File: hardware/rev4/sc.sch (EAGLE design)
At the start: 88 parts, among them IC1 PB137ACV, IC2 LM2675M-ADJ, Q1 si2305cd, Q2 IRFR5305, Q3 IRFR5305, T1 BC846, T2 BC846, T3 BC846, U1 SPX5205 3v3, X1 prog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

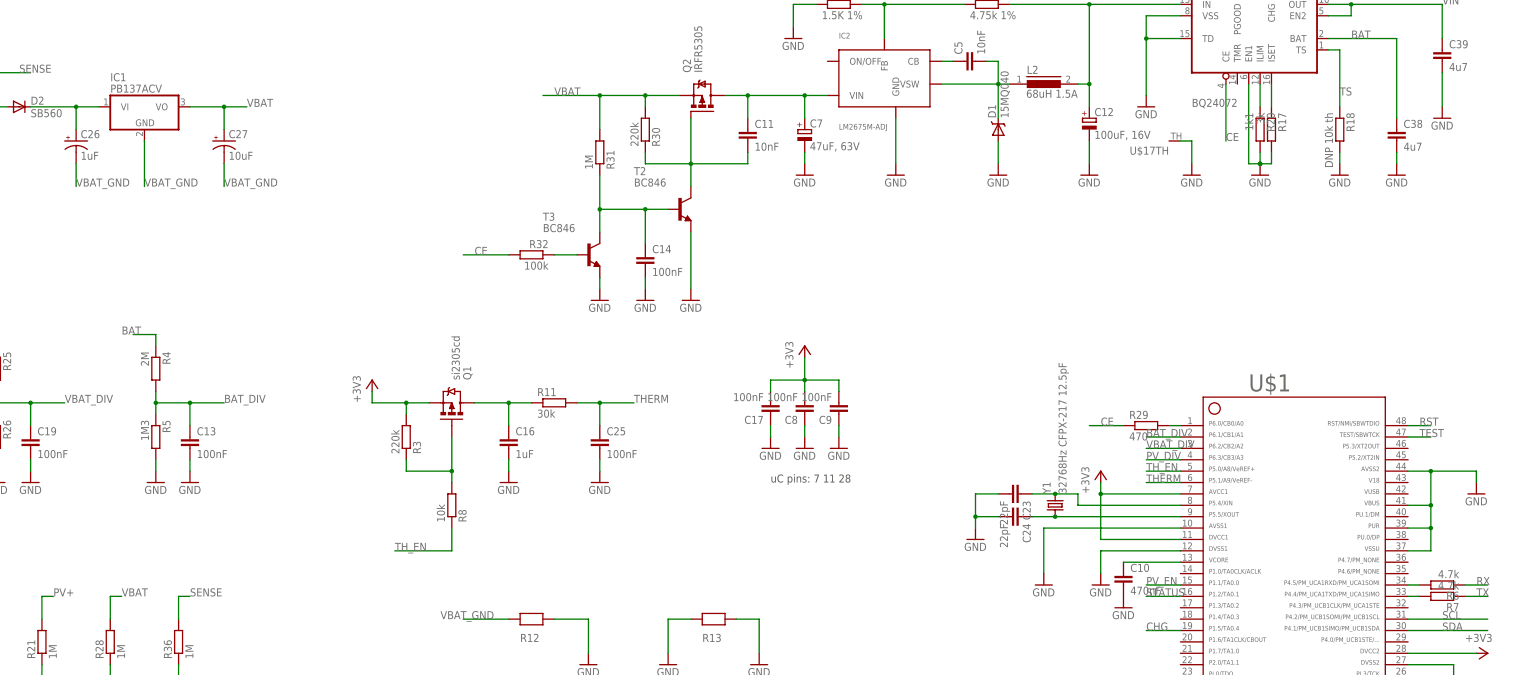
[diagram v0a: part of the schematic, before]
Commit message: control pins working
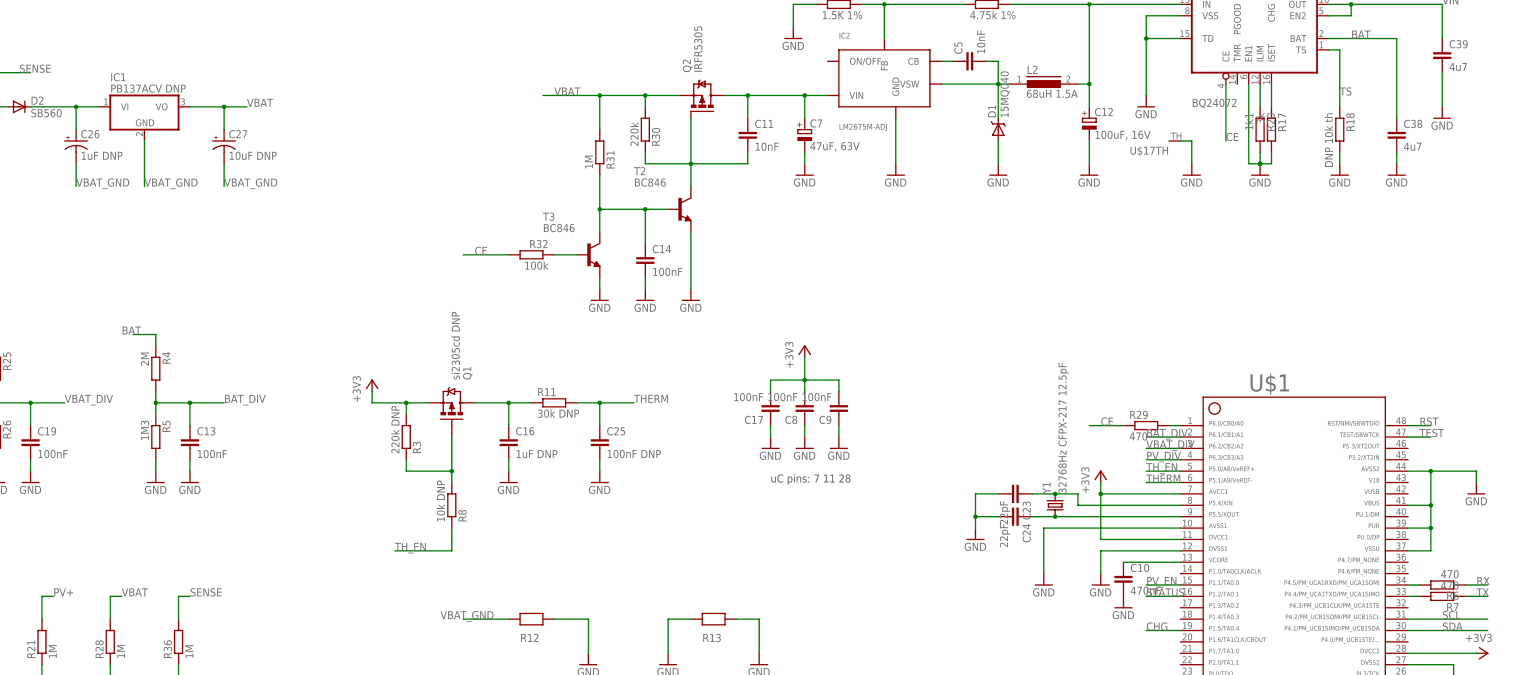
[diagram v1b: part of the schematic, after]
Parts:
- C16, C26: value 1uF -> 1uF DNP
- C25: value 100nF -> 100nF DNP
- C27: value 10uF -> 10uF DNP
- IC1: value PB137ACV -> PB137ACV DNP
- Q1: value si2305cd -> si2305cd DNP
- R11: value 30k -> 30k DNP
- R3: value 220k -> 220k DNP
- R6, R7: value 4.7k -> 470
- R8: value 10k -> 10k DNP
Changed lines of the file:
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@@
 <part name="GND22" library="SparkFun" deviceset="GND" device=""/>
 <part name="C10" library="rcl" deviceset="C-EU" device="C0805" value="470nF"/>
-<part name="R6" library="rcl" deviceset="R-EU_" device="R0805W" value="4.7k"/>
-<part name="R7" library="rcl" deviceset="R-EU_" device="R0805W" value="4.7k"/>
+<part name="R6" library="rcl" deviceset="R-EU_" device="R0805W" value="470"/>
+<part name="R7" library="rcl" deviceset="R-EU_" device="R0805W" value="470"/>
 <part name="Y1" library="Simplex-FreqCtrl" deviceset="CRYSTAL" device="3.2X1.5" value="32768Hz CFPX-217 12.5pF"/>
 <part name="C23" library="rcl" deviceset="C-EU" device="C0805" value="22pF"/>
@@
 <part name="R26" library="rcl" deviceset="R-EU_" device="R0805W" value="330k"/>
 <part name="GND34" library="SparkFun" deviceset="GND" device=""/>
-<part name="R3" library="rcl" deviceset="R-EU_" device="R0805W" value="220k"/>
-<part name="Q1" library="Simplex-DiscreteSemi" deviceset="MOSFET-PCHANNEL" device="SMD_POWER" value="si2305cd"/>
-<part name="R8" library="rcl" deviceset="R-EU_" device="R0805W" value="10k"/>
+<part name="R3" library="rcl" deviceset="R-EU_" device="R0805W" value="220k DNP"/>
+<part name="Q1" library="Simplex-DiscreteSemi" deviceset="MOSFET-PCHANNEL" device="SMD_POWER" value="si2305cd DNP"/>
+<part name="R8" library="rcl" deviceset="R-EU_" device="R0805W" value="10k DNP"/>
 <part name="C17" library="rcl" deviceset="C-EU" device="C0805" value="100nF"/>
 <part name="GND32" library="SparkFun" deviceset="GND" device=""/>
@@
 <part name="GND40" library="SparkFun" deviceset="GND" device=""/>
 <part name="GND41" library="SparkFun" deviceset="GND" device=""/>
-<part name="IC1" library="linear" deviceset="78*" device="TV" technology="12" value="PB137ACV"/>
+<part name="IC1" library="linear" deviceset="78*" device="TV" technology="12" value="PB137ACV DNP"/>
 <part name="Q3" library="transistor-power" deviceset="IRF?5305" device="R"/>
 <part name="R2" library="rcl" deviceset="R-EU_" device="R0805W" value="10k"/>
-<part name="R11" library="rcl" deviceset="R-EU_" device="R0805W" value="30k"/>
-<part name="C25" library="rcl" deviceset="C-EU" device="C0805" value="100nF"/>
+<part name="R11" library="rcl" deviceset="R-EU_" device="R0805W" value="30k DNP"/>
+<part name="C25" library="rcl" deviceset="C-EU" device="C0805" value="100nF DNP"/>
 <part name="GND8" library="SparkFun" deviceset="GND" device=""/>
 <part name="JP2" library="SparkFun-Connectors" deviceset="M02" device="PTH" value="thermistor"/>
-<part name="C27" library="SparkFun-Capacitors" deviceset="CAP_POL" device="D" value="10uF"/>
-<part name="C26" library="SparkFun-Capacitors" deviceset="CAP_POL" device="D" value="1uF"/>
+<part name="C27" library="SparkFun-Capacitors" deviceset="CAP_POL" device="D" value="10uF DNP"/>
+<part name="C26" library="SparkFun-Capacitors" deviceset="CAP_POL" device="D" value="1uF DNP"/>
 <part name="R21" library="rcl" deviceset="R-EU_" device="R0805W" value="1M"/>
 <part name="LED6" library="led" deviceset="LED" device="CHIP-LED0805" value="green"/>
@@
 <part name="Q2" library="transistor-power" deviceset="IRF?5305" device="R"/>
 <part name="GND15" library="SparkFun" deviceset="GND" device=""/>
-<part name="C16" library="rcl" deviceset="C-EU" device="C0805" value="1uF"/>
+<part name="C16" library="rcl" deviceset="C-EU" device="C0805" value="1uF DNP"/>
 <part name="R23" library="rcl" deviceset="R-EU_" device="R0805W" value="4.7k"/>
 <part name="R27" library="rcl" deviceset="R-EU_" device="R0805W" value="4.7k"/>

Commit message: adc, rtc work
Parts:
- R22: value 2M -> 1M2
- R24: value 220k -> 100k
- R32: value 100k -> DNP 100k
- R4: value 2M -> 680K
- R5: value 1M3 -> 330k
- R9: value 4.75k 1% -> 4K3
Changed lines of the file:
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@@
 <part name="R16" library="rcl" deviceset="R-EU_" device="R0805W" value="100k"/>
 <part name="R19" library="rcl" deviceset="R-EU_" device="R0805W" value="220k"/>
-<part name="R22" library="rcl" deviceset="R-EU_" device="R0805W" value="2M"/>
-<part name="R24" library="rcl" deviceset="R-EU_" device="R0805W" value="220k"/>
+<part name="R22" library="rcl" deviceset="R-EU_" device="R0805W" value="1M2"/>
+<part name="R24" library="rcl" deviceset="R-EU_" device="R0805W" value="100k"/>
 <part name="R25" library="rcl" deviceset="R-EU_" device="R0805W" value="2M"/>
 <part name="R26" library="rcl" deviceset="R-EU_" device="R0805W" value="330k"/>
@@
 <part name="GND7" library="supply1" deviceset="GND" device=""/>
 <part name="R1" library="rcl" deviceset="R-EU_" device="R0805W" value="1.5K 1%"/>
-<part name="R9" library="rcl" deviceset="R-EU_" device="R0805W" value="4.75k 1%"/>
+<part name="R9" library="rcl" deviceset="R-EU_" device="R0805W" value="4K3"/>
 <part name="C5" library="rcl" deviceset="C-EU" device="C0805" value="10nF"/>
 <part name="GND12" library="supply1" deviceset="GND" device=""/>
@@
 <part name="R23" library="rcl" deviceset="R-EU_" device="R0805W" value="4.7k"/>
 <part name="R27" library="rcl" deviceset="R-EU_" device="R0805W" value="4.7k"/>
-<part name="R4" library="rcl" deviceset="R-EU_" device="R0805W" value="2M"/>
-<part name="R5" library="rcl" deviceset="R-EU_" device="R0805W" value="1M3"/>
+<part name="R4" library="rcl" deviceset="R-EU_" device="R0805W" value="680K"/>
+<part name="R5" library="rcl" deviceset="R-EU_" device="R0805W" value="330k"/>
 <part name="C13" library="rcl" deviceset="C-EU" device="C0805" value="100nF"/>
 <part name="GND1" library="SparkFun" deviceset="GND" device=""/>
@@
 <part name="T3" library="transistor" deviceset="BC846" device=""/>
 <part name="R31" library="rcl" deviceset="R-EU_" device="R0805W" value="1M"/>
-<part name="R32" library="rcl" deviceset="R-EU_" device="R0805W" value="100k"/>
+<part name="R32" library="rcl" deviceset="R-EU_" device="R0805W" value="DNP 100k"/>
 <part name="C14" library="rcl" deviceset="C-EU" device="C0805" value="100nF"/>
 <part name="GND25" library="SparkFun" deviceset="GND" device=""/>

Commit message: testing stage
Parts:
- R17: value 3k -> 8k9
- R20: value 1k1 -> 8k
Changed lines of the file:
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@@
 <part name="GND51" library="SparkFun" deviceset="GND" device=""/>
 <part name="GND57" library="SparkFun" deviceset="GND" device=""/>
-<part name="R17" library="rcl" deviceset="R-EU_" device="R0805W" value="3k"/>
+<part name="R17" library="rcl" deviceset="R-EU_" device="R0805W" value="8k9"/>
 <part name="R18" library="rcl" deviceset="R-EU_" device="R0805W" value="DNP 10k th"/>
 <part name="GND58" library="SparkFun" deviceset="GND" device=""/>
-<part name="R20" library="rcl" deviceset="R-EU_" device="R0805W" value="1k1"/>
+<part name="R20" library="rcl" deviceset="R-EU_" device="R0805W" value="8k"/>
 <part name="GND59" library="SparkFun" deviceset="GND" device=""/>
 <part name="C38" library="rcl" deviceset="C-EU" device="C1206" value="4u7"/>

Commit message: add README files
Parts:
- D2: value SB560 -> SB560 DNP
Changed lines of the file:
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@@
 <part name="R36" library="rcl" deviceset="R-EU_" device="R0805W" value="1M"/>
 <part name="LED8" library="led" deviceset="LED" device="CHIP-LED0805" value="green"/>
-<part name="D2" library="diode" deviceset="DIODE-" device="C1702-05" value="SB560"/>
+<part name="D2" library="diode" deviceset="DIODE-" device="C1702-05" value="SB560 DNP"/>
 <part name="IC2" library="Simplex-ICs" deviceset="LM2674" device="" value="LM2675M-ADJ"/>
 <part name="GND7" library="supply1" deviceset="GND" device=""/>
